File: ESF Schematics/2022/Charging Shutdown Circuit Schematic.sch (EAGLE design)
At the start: 58 parts

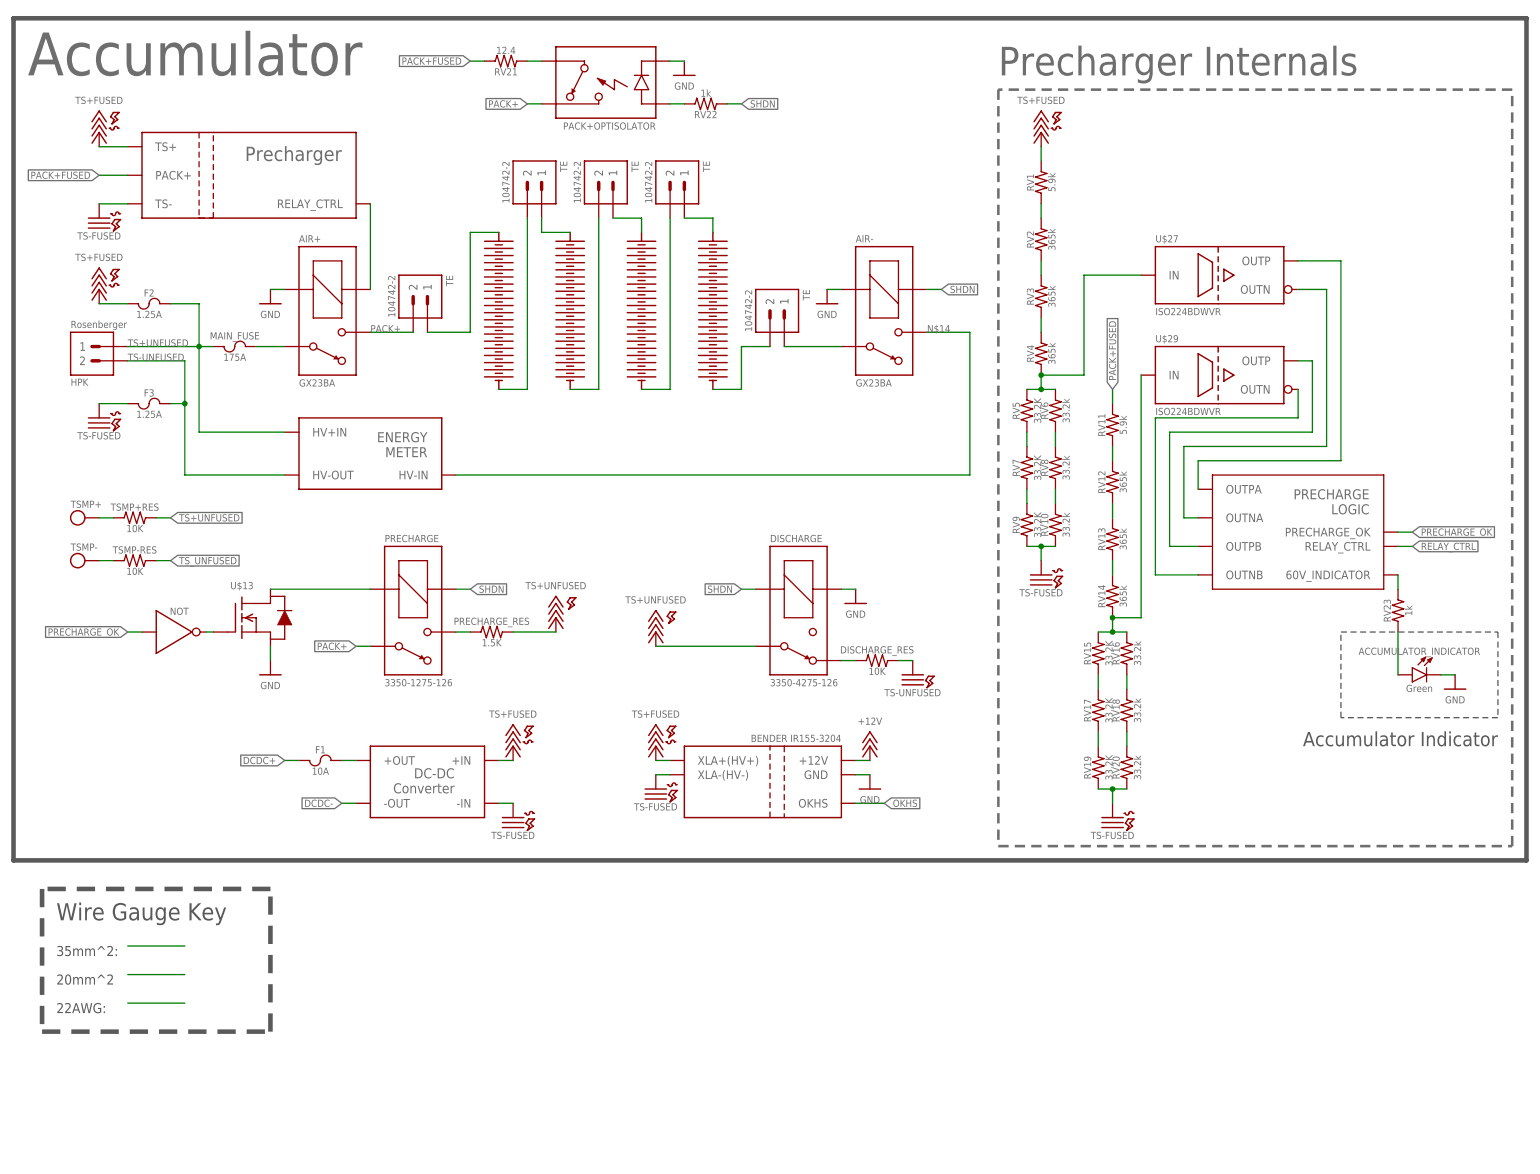
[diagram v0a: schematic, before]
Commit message: started charger shutdown schem
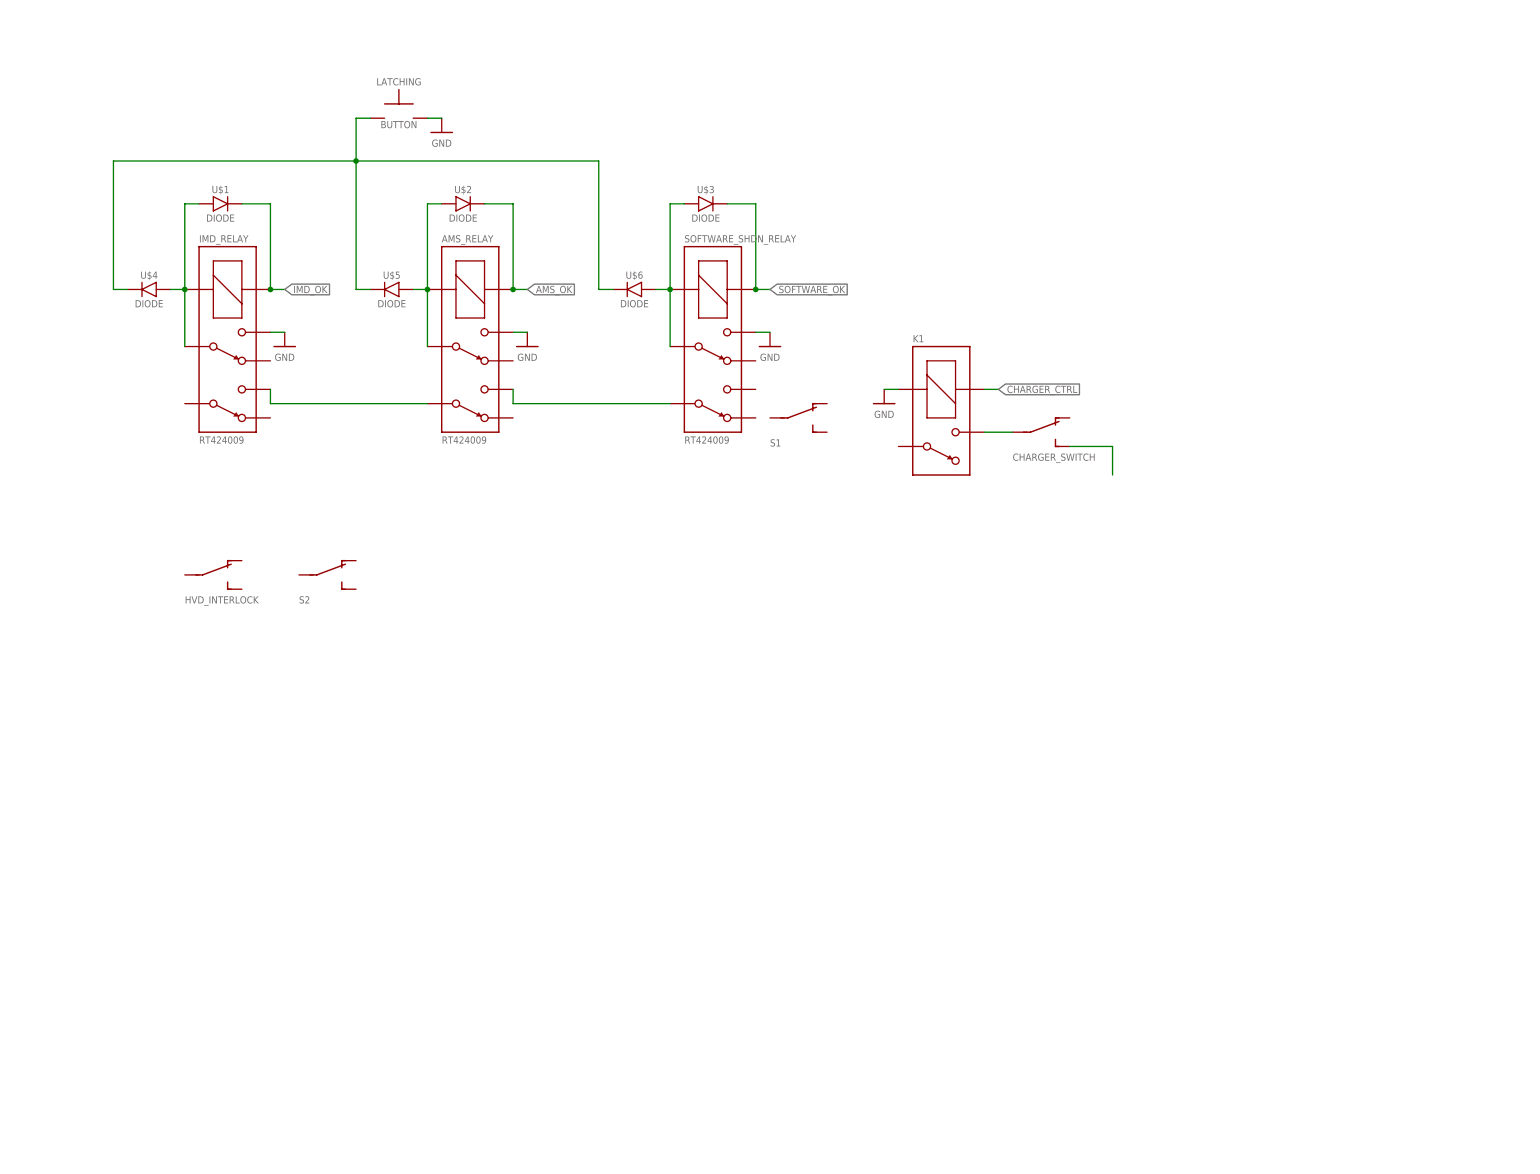
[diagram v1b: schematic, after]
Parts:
- removed ACCUMULATOR_INDICATOR: LED_0603_GREEN, HyTechDevices:LED_0603_GREEN
- removed AIR+, AIR-: RELAY_SPST_NO_GX23BA, HyTechSymbolsTemp:RELAY_SPST_NO_GX23BA
- removed DISCHARGE: RELAY_SPST_NC_3350-4275-126, HyTechSymbolsTemp:RELAY_SPST_NC_3350-4275-126
- removed DISCHARGE_RES, TSMP+RES, TSMP-RES: 10K, HyTechDevices:RESISTOR_VALUE
- removed F1: 10A, HyTechSymbolsTemp:FUSE
- removed F2, F3: 1.25A, HyTechSymbolsTemp:FUSE
- removed MAIN_FUSE: 175A, HyTechSymbolsTemp:FUSE
- removed PACK+OPTISOLATOR: RELAY_SOLIDSTATE_NO, HyTechSymbolsTemp:RELAY_SOLIDSTATE_NO
- removed PRECHARGE: RELAY_SPST_NO_3350-1275-126, HyTechSymbolsTemp:RELAY_SPST_NO_3350-1275-126
- removed PRECHARGE_RES: 1.5K, HyTechDevices:RESISTOR_VALUE
- removed RV1, RV11: 5.9k, HyTechDevices:RESISTOR_VALUE
- removed RV10, RV16, RV18, RV20, RV6, RV8: 33.2k, HyTechDevices:RESISTOR_VALUE
- removed RV12, RV13, RV14, RV2, RV3, RV4: 365k, HyTechDevices:RESISTOR_VALUE
- removed RV15, RV17, RV19, RV5, RV7, RV9: 33.2K, HyTechDevices:RESISTOR_VALUE
- removed RV21: 12.4, HyTechDevices:RESISTOR_VALUE
- removed RV22, RV23: 1k, HyTechDevices:RESISTOR_VALUE
- removed TSMP+, TSMP-: TEST_POINT, HyTechDevices:TEST_POINT
- removed U$10: CONNECTOR-2_HPK, HyTechSymbolsTemp:CONNECTOR-2_HPK
- removed U$11: PRECHARGER, HyTechSymbolsTemp:PRECHARGER
- removed U$12: LOGICGATE_INVERTER, HyTechSymbolsTemp:LOGICGATE_INVERTER
- removed U$13: MOSFET_N-CHANNEL, HyTechSymbolsTemp:MOSFET_N-CHANNEL
- removed U$14: ENERGY_METER, HyTechSymbolsTemp:ENERGY_METER
- removed U$15, U$16, U$7, U$8, U$9: CONNECTOR-2_104742-2, HyTechSymbolsTemp:CONNECTOR-2_104742-2
- removed U$27, U$29: ISO_224BDWVR, HyTechSymbolsTemp:ISO_224BDWVR
- removed U$30: PRECHARGE_LOGIC, HyTechSymbolsTemp:PRECHARGE_LOGIC
- added AMS_RELAY, IMD_RELAY, SOFTWARE_SHDN_RELAY: RELAY_DPDT_RT424009, HyTechSymbolsTemp:RELAY_DPDT_RT424009
- added CHARGER_SWITCH, HVD_INTERLOCK, S1, S2: SWITCH_SPST, HyTechSymbols:SWITCH_SPST
- added K1: RELAY_SPST_NO_, HyTechSymbolsTemp:RELAY_SPST_NO_
- added LATCHING: BUTTON_NO, HyTechSymbolsTemp:BUTTON_NO
- U$1: value BENDER_IR155-3204 -> DIODE; device HyTechSymbols:BENDER_IR155-3204 -> HyTechSymbolsTemp:DIODE
- U$2: value DC-DC_CONVERTER -> DIODE; device HyTechSymbols:DC-DC_CONVERTER -> HyTechSymbolsTemp:DIODE
- U$3, U$4, U$5, U$6: value SEGMENT -> DIODE; device HyTechSymbols:SEGMENT -> HyTechSymbolsTemp:DIODE
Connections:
- removed net +12V: U$1.+12V
- removed net DCDC+: F1.1
- removed net DCDC-: U$2.-OUT
- removed net N$12: DISCHARGE.CONTACT2, DISCHARGE_RES.1
- removed net N$13: PRECHARGE.COIL+, U$13.D
- removed net N$14: AIR-.CONTACT2, U$14.HV-IN
- removed net N$15: RV1.1, RV2.2
- removed net N$16: AIR-.CONTACT1, U$15.1
- removed net N$17: AIR+.CONTACT2, U$16.2
- removed net N$18: F1.2, U$2.+OUT
- removed net N$19: RV2.1, RV3.2
- removed net N$20: RV3.1, RV4.2
- removed net N$21: RV4.1, RV5.2, RV6.2, U$27.IN
- removed net N$22: RV6.1, RV8.2
- removed net N$23: RV5.1, RV7.2
- removed net N$24: RV7.1, RV9.2
- removed net N$25: RV10.2, RV8.1
- removed net N$26: RV11.1, RV12.2
- removed net N$27: RV12.1, RV13.2
- removed net N$28: RV13.1, RV14.2
- removed net N$29: RV14.1, RV15.2, RV16.2, U$29.IN
- removed net N$30: RV16.1, RV18.2
- removed net N$31: RV15.1, RV17.2
- removed net N$32: RV17.1, RV19.2
- removed net N$33: RV18.1, RV20.2
- removed net N$34: U$29.OUTN, U$30.OUTNB
- removed net N$35: U$29.OUTP, U$30.OUTPB
- removed net N$36: U$27.OUTN, U$30.OUTNA
- removed net N$37: U$27.OUTP, U$30.OUTPA
- removed net N$38: PACK+OPTISOLATOR.CONTROL+, RV22.2
- removed net N$40: PACK+OPTISOLATOR.CONTACT1, RV21.1
- removed net N$43: RV23.2, U$30.60V_INDICATOR
- removed net N$44: ACCUMULATOR_INDICATOR.A, RV23.1
- removed net N$7: U$15.2, U$6.-
- removed net N$8: PRECHARGE.CONTACT2, PRECHARGE_RES.1
- removed net N$9: TSMP+.P$1, TSMP+RES.1
- removed net OKHS: U$1.OKHS
- removed net PACK+: PACK+OPTISOLATOR.CONTACT2, PRECHARGE.CONTACT1, U$16.1, U$3.+
- removed net PACK+FUSED: RV11.2, RV21.2, U$11.PACK+
- removed net PRECHARGE_OK: U$12.IN, U$30.PRECHARGE_OK
- removed net RELAY_CTRL: AIR+.COIL-, U$11.RELAY_CTRL, U$30.RELAY_CTRL
- removed net SHDN: AIR-.COIL-, DISCHARGE.COIL+, PRECHARGE.COIL-, RV22.1
- removed net TS+: F2.1, RV1.2, U$1.XLA+(HV+), U$11.TS+, U$2.+IN
- removed net TS+UNFUSED: AIR+.CONTACT1, DISCHARGE.CONTACT1, F2.2, MAIN_FUSE.1, MAIN_FUSE.2, PRECHARGE_RES.2, TSMP+RES.2, U$10.1, U$14.HV+IN
- removed net TS-UNFUSED: DISCHARGE_RES.2, F3.1, F3.2, RV10.1, RV19.1, RV20.1, RV9.1, U$1.XLA-(HV-), U$10.2, U$11.TS-, U$14.HV-OUT, U$2.-IN
- removed net TS_UNFUSED: TSMP-RES.2
- new net AMS_OK: AMS_RELAY.COIL+, U$2.C
- new net CHARGER_CTRL: K1.COIL-
- new net IMD_OK: IMD_RELAY.COIL+, U$1.C
- new net SOFTWARE_OK: SOFTWARE_SHDN_RELAY.COIL+, U$3.C
- net GND: now also AMS_RELAY.4, IMD_RELAY.4, K1.COIL+, LATCHING.P$2, SOFTWARE_SHDN_RELAY.4; no longer ACCUMULATOR_INDICATOR.C, AIR+.COIL+, AIR-.COIL+, DISCHARGE.COIL-, PACK+OPTISOLATOR.CONTROL-, U$1.GND, U$13.S
- net N$1: now also IMD_RELAY.3, IMD_RELAY.COIL-, U$1.A, U$4.A; no longer U$3.-, U$7.2
- net N$10: now also AMS_RELAY.5, SOFTWARE_SHDN_RELAY.6; no longer TSMP-.P$1, TSMP-RES.1
- net N$11: now also AMS_RELAY.6, IMD_RELAY.5; no longer U$12.!IN, U$13.G
- net N$2: now also LATCHING.P$1, U$4.C, U$5.C, U$6.C; no longer U$4.-, U$8.2
- net N$3: now also AMS_RELAY.3, AMS_RELAY.COIL-, U$2.A, U$5.A; no longer U$5.-, U$9.2
- net N$4: now also CHARGER_SWITCH.P, K1.CONTACT2; no longer U$4.+, U$7.1
- net N$5: now also SOFTWARE_SHDN_RELAY.3, SOFTWARE_SHDN_RELAY.COIL-, U$3.A, U$6.A; no longer U$5.+, U$8.1
- net N$6: now also CHARGER_SWITCH.S; no longer U$6.+, U$9.1
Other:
- note removed: "20mm^2"
- note removed: "22AWG:"
- note removed: "35mm^2:"
- note removed: "Accumulator"
- note removed: "Accumulator Indicator"
- note removed: "Precharger Internals"
- note removed: "Wire Gauge Key"

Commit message: Further progress on charging shutdown circuit
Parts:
- removed S2: SWITCH_SPST, HyTechSymbols:SWITCH_SPST
- added AIR1, AIR2: RELAY_SPST_NO_GX23BA, HyTechSymbolsTemp:RELAY_SPST_NO_GX23BA
- added F1, F2: 10A, HyTechSymbolsTemp:FUSE
- added HPK_INTERLOCK: SWITCH_SPST, HyTechSymbols:SWITCH_SPST
- added J1, J2: CONNECTOR-2_HPK, HyTechSymbolsTemp:CONNECTOR-2_HPK
- added U$7: PRECHARGER, HyTechSymbolsTemp:PRECHARGER
- added U$8: CHARGER_G4-0017-01, HyTechSymbolsTemp:CHARGER_G4-0017-01
- renumbered S1 to CHARGER_ESTOP
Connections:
- new net N$12: AIR1.CONTACT1, J1.1, U$7.TS+
- new net N$13: AIR2.CONTACT2, J1.2, U$7.TS-
- new net N$14: F1.1, J2.1
- new net N$15: F2.1, J2.2
- new net N$16: F1.2, U$8.TS+
- new net N$17: F2.2, U$8.TS-
- new net N$7: CHARGER_ESTOP.P, SOFTWARE_SHDN_RELAY.7
- new net N$8: CHARGER_ESTOP.O, HVD_INTERLOCK.P
- new net N$9: HPK_INTERLOCK.P, HVD_INTERLOCK.S
- new net PACK+: AIR1.CONTACT2, U$7.PACK+
- new net PACK-: AIR2.CONTACT1
- new net RELAY_CTRL: AIR1.COIL-, U$7.RELAY_CTRL
- new net SHDN: AIR2.COIL-, HPK_INTERLOCK.S, U$7.12V
- net GND: now also AIR1.COIL+, AIR2.COIL+, U$7.GND
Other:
- moved on the sheet: CHARGER_SWITCH, HVD_INTERLOCK, K1

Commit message: More schematic updates
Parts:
- added J3, J4, J5, J6: CONNECTOR-1_LCAX2-14F-E, HyTechSymbolsTemp:CONNECTOR-1_LCAX2-14F-E
- added J7: CONNECTOR-3_NEMA-5-15, HyTechSymbolsTemp:CONNECTOR-3_NEMA-5-15
- added U$9: POWER_RELAY, HyTechSymbolsTemp:POWER_RELAY
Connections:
- new net CHARGER_CONTROLLER_CANH: U$8.CANH
- new net CHARGER_CONTROLLER_CANL: U$8.CANL
- new net N$18: J1.1, J3.1
- new net N$19: J1.2, J4.1
- new net N$20: U$8.HOT, U$9.HOT_OUT
- new net N$21: U$8.NEUTRAL, U$9.NEUTRAL_OUT
- new net N$22: U$8.GND, U$9.GND_OUT
- new net N$23: J7.1, U$9.HOTIN
- new net N$24: J7.2, U$9.NEUTRAL_IN
- new net N$25: J7.3, U$9.GND_IN
- new net N$26: HVD_INTERLOCK.P
- net N$12: now also J6.1; no longer J1.1
- net N$13: now also J5.1; no longer J1.2
- net N$8: no longer HVD_INTERLOCK.P
- net SHDN: now also U$7.VCC, U$9.EN; no longer U$7.12V
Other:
- note added: "ACCUMULATOR"
- moved on the sheet: AIR1, AIR2, AMS_RELAY, CHARGER_ESTOP, F1, F2, HPK_INTERLOCK, HVD_INTERLOCK, IMD_RELAY, LATCHING, SOFTWARE_SHDN_RELAY, U$1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

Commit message: final drafts of most schematics
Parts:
- added J8, J9: CONNECTOR-3_HV02-M3S(40A), HyTechSymbolsTemp:CONNECTOR-3_HV02-M3S(40A)
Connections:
- removed net N$26: HVD_INTERLOCK.P
- new net N$31: J9.3, U$9.GND_OUT
- new net N$32: J9.2, U$9.NEUTRAL_OUT
- new net N$33: J9.1, U$9.HOT_OUT
- net N$20: now also J8.1; no longer U$9.HOT_OUT
- net N$21: now also J8.2; no longer U$9.NEUTRAL_OUT
- net N$22: now also J8.3; no longer U$9.GND_OUT
- net N$8: now also HVD_INTERLOCK.P
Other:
- note added: "17.5mm^2"
- note added: "17.5mm^2:"
- note added: "22AWG"
- note added: "22AWG:"
- note added: "35mm^2"
- note added: "35mm^2:"
- note added: "6mm^2"
- note added: "6mm^2:"
- note added: "Wire Gauge Key"
- moved on the sheet: AIR1, AIR2, F1, F2, HPK_INTERLOCK, HVD_INTERLOCK

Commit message: ESF review changes
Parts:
- removed CHARGER_SWITCH: SWITCH_SPST, HyTechSymbols:SWITCH_SPST
- removed F1, F2: 10A, HyTechSymbolsTemp:FUSE
- removed K1: RELAY_SPST_NO_, HyTechSymbolsTemp:RELAY_SPST_NO_
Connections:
- removed net CHARGER_CTRL: K1.COIL-
- removed net N$14: F1.1, J2.1
- removed net N$15: F2.1, J2.2
- removed net N$4: CHARGER_SWITCH.P, K1.CONTACT2
- removed net N$6: CHARGER_SWITCH.S
- net GND: no longer K1.COIL+
- net N$16: now also J2.1; no longer F1.2
- net N$17: now also J2.2; no longer F2.2
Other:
- note added: "HVD connectors busbar labelling add PS to relay for shdn charger controller box move interlocks outside accumulator"
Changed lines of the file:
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@@
 <part name="P3" library="HyTechSupplies" deviceset="GND" device=""/>
 <part name="LATCHING" library="HyTechSymbolsTemp" deviceset="BUTTON_NO" device=""/>
-<part name="K1" library="HyTechSymbolsTemp" deviceset="RELAY_SPST_NO_?*" device=""/>
-<part name="P5" library="HyTechSupplies" deviceset="GND" device=""/>
-<part name="CHARGER_SWITCH" library="HyTechSymbols" deviceset="SWITCH_SPST" device=""/>
 <part name="HVD_INTERLOCK" library="HyTechSymbols" deviceset="SWITCH_SPST" device=""/>
 <part name="HPK_INTERLOCK" library="HyTechSymbols" deviceset="SWITCH_SPST" device=""/>
@@
 <part name="J1" library="HyTechSymbolsTemp" deviceset="CONNECTOR-2_*" device="" technology="HPK"/>
 <part name="J2" library="HyTechSymbolsTemp" deviceset="CONNECTOR-2_*" device="" technology="HPK"/>
-<part name="F1" library="HyTechSymbolsTemp" deviceset="FUSE" device="" value="10A"/>
-<part name="F2" library="HyTechSymbolsTemp" deviceset="FUSE" device="" value="10A"/>
 <part name="U$8" library="HyTechSymbolsTemp" deviceset="CHARGER_*" device="" technology="G4-0017-01"/>
 <part name="U$7" library="HyTechSymbolsTemp" deviceset="PRECHARGER" device=""/>
@@
 <text x="91.44" y="99.06" size="1.27" layer="97" align="top-left">17.5mm^2</text>
 <text x="96.52" y="76.2" size="1.27" layer="97" align="top-left">17.5mm^2</text>
+<text x="162.56" y="142.24" size="1.778" layer="88">HVD connectors
+busbar labelling
+add PS to relay for shdn
+charger controller box
+move interlocks outside accumulator</text>
 </plain>
 <instances>
@@
 <attribute name="NAME" x="71.12" y="203.962" size="1.27" layer="95" align="bottom-center"/>
 </instance>
-<instance part="K1" gate="G$1" x="177.8" y="152.4" smashed="yes">
-<attribute name="MPN" x="177.8" y="128.778" size="1.27" layer="96" align="top-left"/>
-<attribute name="NAME" x="177.8" y="153.162" size="1.27" layer="95"/>
-</instance>
-<instance part="P5" gate="1" x="172.72" y="142.24" smashed="yes">
-<attribute name="VALUE" x="172.72" y="140.97" size="1.27" layer="96" align="top-center"/>
-</instance>
-<instance part="CHARGER_SWITCH" gate="SPST" x="200.66" y="137.16" smashed="yes" rot="R270">
-<attribute name="NAME" x="185.42" y="132.08" size="1.27" layer="96"/>
-</instance>
 <instance part="HVD_INTERLOCK" gate="SPST" x="30.48" y="124.46" smashed="yes" rot="R270">
 <attribute name="NAME" x="25.4" y="119.38" size="1.27" layer="96"/>
@@
 <attribute name="MPN" x="154.94" y="88.265" size="1.27" layer="96" align="top-left"/>
 <attribute name="MANUFACTURER" x="154.94" y="97.282" size="1.27" layer="95"/>
-</instance>
-<instance part="F1" gate="G$1" x="172.72" y="93.98" smashed="yes">
-<attribute name="NAME" x="171.45" y="95.25" size="1.27" layer="95" align="bottom-center"/>
-<attribute name="VALUE" x="171.45" y="92.71" size="1.27" layer="96" align="top-center"/>
-</instance>
-<instance part="F2" gate="G$1" x="180.34" y="88.9" smashed="yes">
-<attribute name="NAME" x="179.07" y="90.17" size="1.27" layer="95" align="bottom-center"/>
-<attribute name="VALUE" x="179.07" y="87.63" size="1.27" layer="96" align="top-center"/>
 </instance>
 <instance part="U$8" gate="G$1" x="215.9" y="106.68" smashed="yes" rot="MR0">
@@
 <pinref part="P3" gate="1" pin="GND"/>
 <pinref part="LATCHING" gate="G$1" pin="P$2"/>
-</segment>
-<segment>
-<pinref part="K1" gate="G$1" pin="COIL+"/>
-<wire x1="175.26" y1="144.78" x2="172.72" y2="144.78" width="0.1524" layer="91"/>
-<pinref part="P5" gate="1" pin="GND"/>
 </segment>
 <segment>
@@
 </segment>
 </net>
-<net name="CHARGER_CTRL" class="0">
-<segment>
-<pinref part="K1" gate="G$1" pin="COIL-"/>
-<wire x1="190.5" y1="144.78" x2="193.04" y2="144.78" width="0.1524" layer="91"/>
-<label x="193.04" y="144.78" size="1.27" layer="95" xref="yes"/>
-</segment>
-</net>
-<net name="N$4" class="0">
-<segment>
-<pinref part="K1" gate="G$1" pin="CONTACT2"/>
-<wire x1="190.5" y1="137.16" x2="195.58" y2="137.16" width="0.1524" layer="91"/>
-<pinref part="CHARGER_SWITCH" gate="SPST" pin="P"/>
-</segment>
-</net>
-<net name="N$6" class="0">
-<segment>
-<pinref part="CHARGER_SWITCH" gate="SPST" pin="S"/>
-<wire x1="205.74" y1="134.62" x2="213.36" y2="134.62" width="0.1524" layer="91"/>
-</segment>
-</net>
 <net name="N$7" class="0">
 <segment>
@@
 </segment>
 </net>
-<net name="N$14" class="0">
-<segment>
-<pinref part="J2" gate="G$1" pin="1"/>
-<wire x1="165.1" y1="93.98" x2="167.64" y2="93.98" width="0.889" layer="91"/>
-<pinref part="F1" gate="G$1" pin="1"/>
-</segment>
-</net>
 <net name="N$17" class="0">
 <segment>
-<pinref part="F2" gate="G$1" pin="2"/>
 <pinref part="U$8" gate="G$1" pin="TS-"/>
 <wire x1="187.96" y1="88.9" x2="182.88" y2="88.9" width="0.889" layer="91"/>
-</segment>
-</net>
-<net name="N$15" class="0">
-<segment>
 <pinref part="J2" gate="G$1" pin="2"/>
 <wire x1="165.1" y1="91.44" x2="165.1" y2="88.9" width="0.889" layer="91"/>
-<pinref part="F2" gate="G$1" pin="1"/>
-<wire x1="165.1" y1="88.9" x2="175.26" y2="88.9" width="0.889" layer="91"/>
+<wire x1="165.1" y1="88.9" x2="182.88" y2="88.9" width="0.889" layer="91"/>
 </segment>
 </net>
 <net name="N$16" class="0">
 <segment>
-<pinref part="F1" gate="G$1" pin="2"/>
 <pinref part="U$8" gate="G$1" pin="TS+"/>
 <wire x1="175.26" y1="93.98" x2="187.96" y2="93.98" width="0.889" layer="91"/>
+<pinref part="J2" gate="G$1" pin="1"/>
+<wire x1="165.1" y1="93.98" x2="175.26" y2="93.98" width="0.889" layer="91"/>
 </segment>
 </net>
@@
 </schematic>
 </drawing>
+<compatibility>
+<note version="6.3" minversion="6.2.2" severity="warning">
+Since Version 6.2.2 text objects can contain more than one line,
+which will not be processed correctly with this version.
+</note>
+</compatibility>
 </eagle>
